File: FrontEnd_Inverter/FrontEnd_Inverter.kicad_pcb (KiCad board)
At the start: 4 copper layers, 210 x 127 mm, 80 parts, among them J1 Conn_02x20_Odd_Even, J11 CONN_02X06, P0 CONN_01X03, P10 CONN_01X02, P11 CONN_01X03, P20 CONN_01X02, P7 CONN_01X03, T1 SKiiP_13ACM12V18, U11 ACS758xCB-PFF, U12 ACS758xCB-PFF, U13 ACS758xCB-PFF, U14 ACS758xCB-PFF, U15 ACS758xCB-PFF, U30 ISE0505A-H, U40 ACPL-C87B, U50 ACPL-C87B

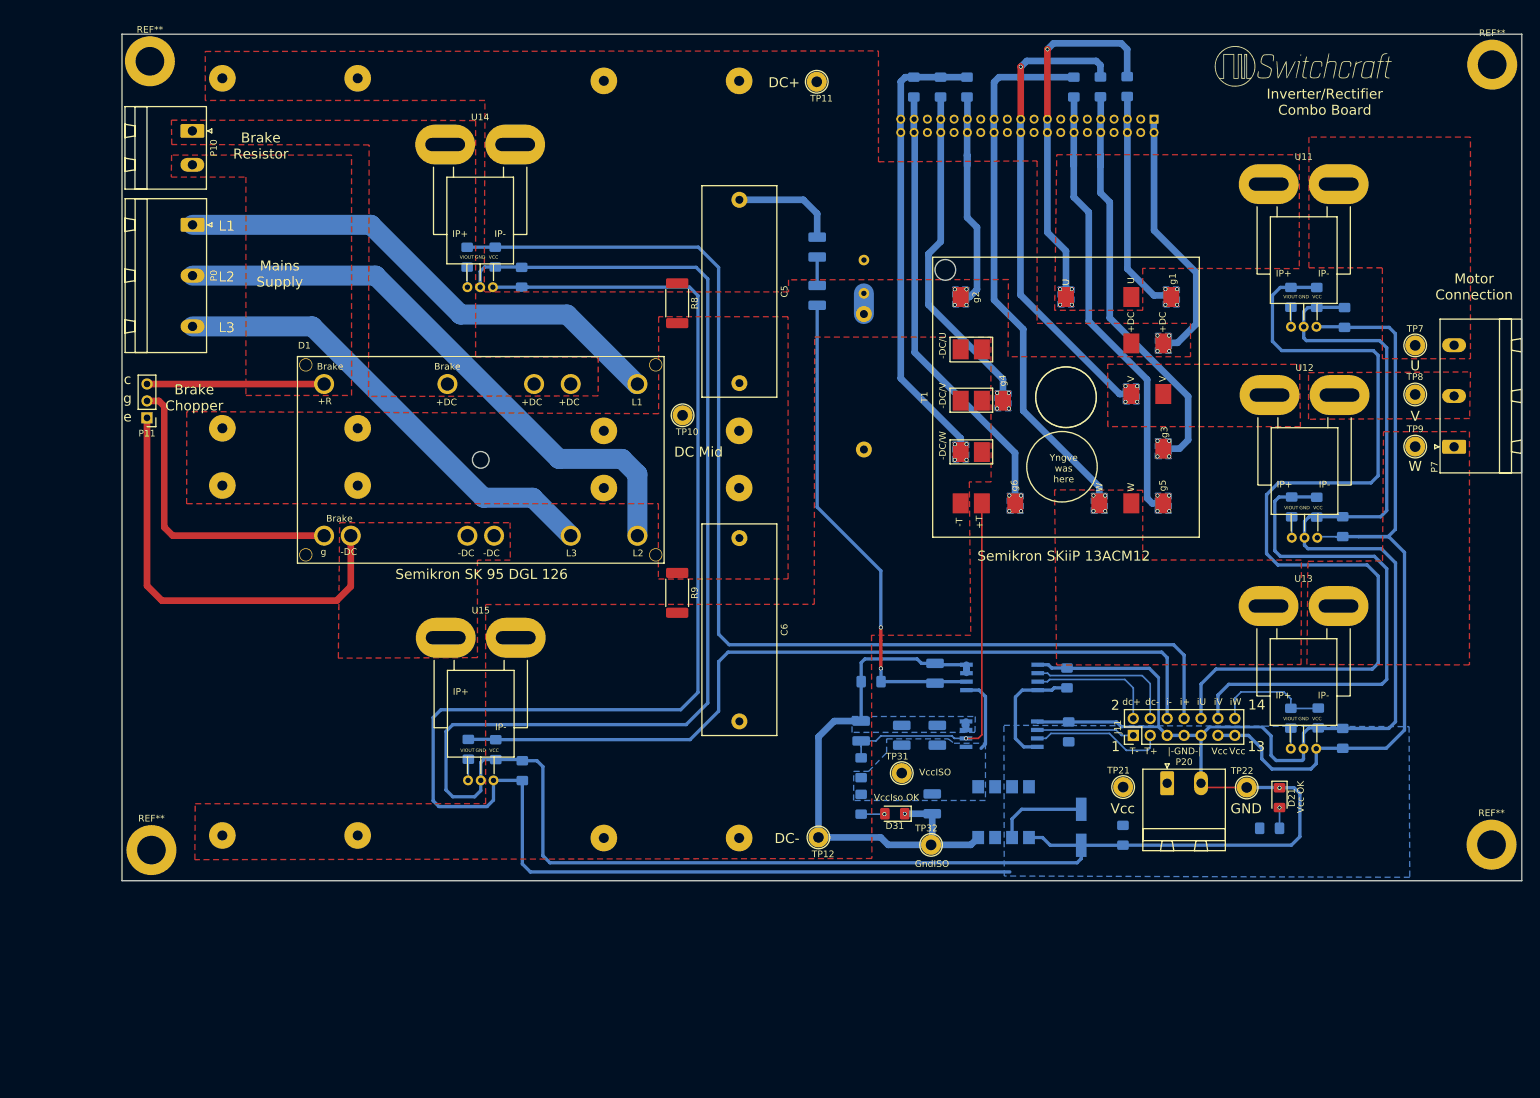
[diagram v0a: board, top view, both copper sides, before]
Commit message: Changed current sensor. Work in progress.
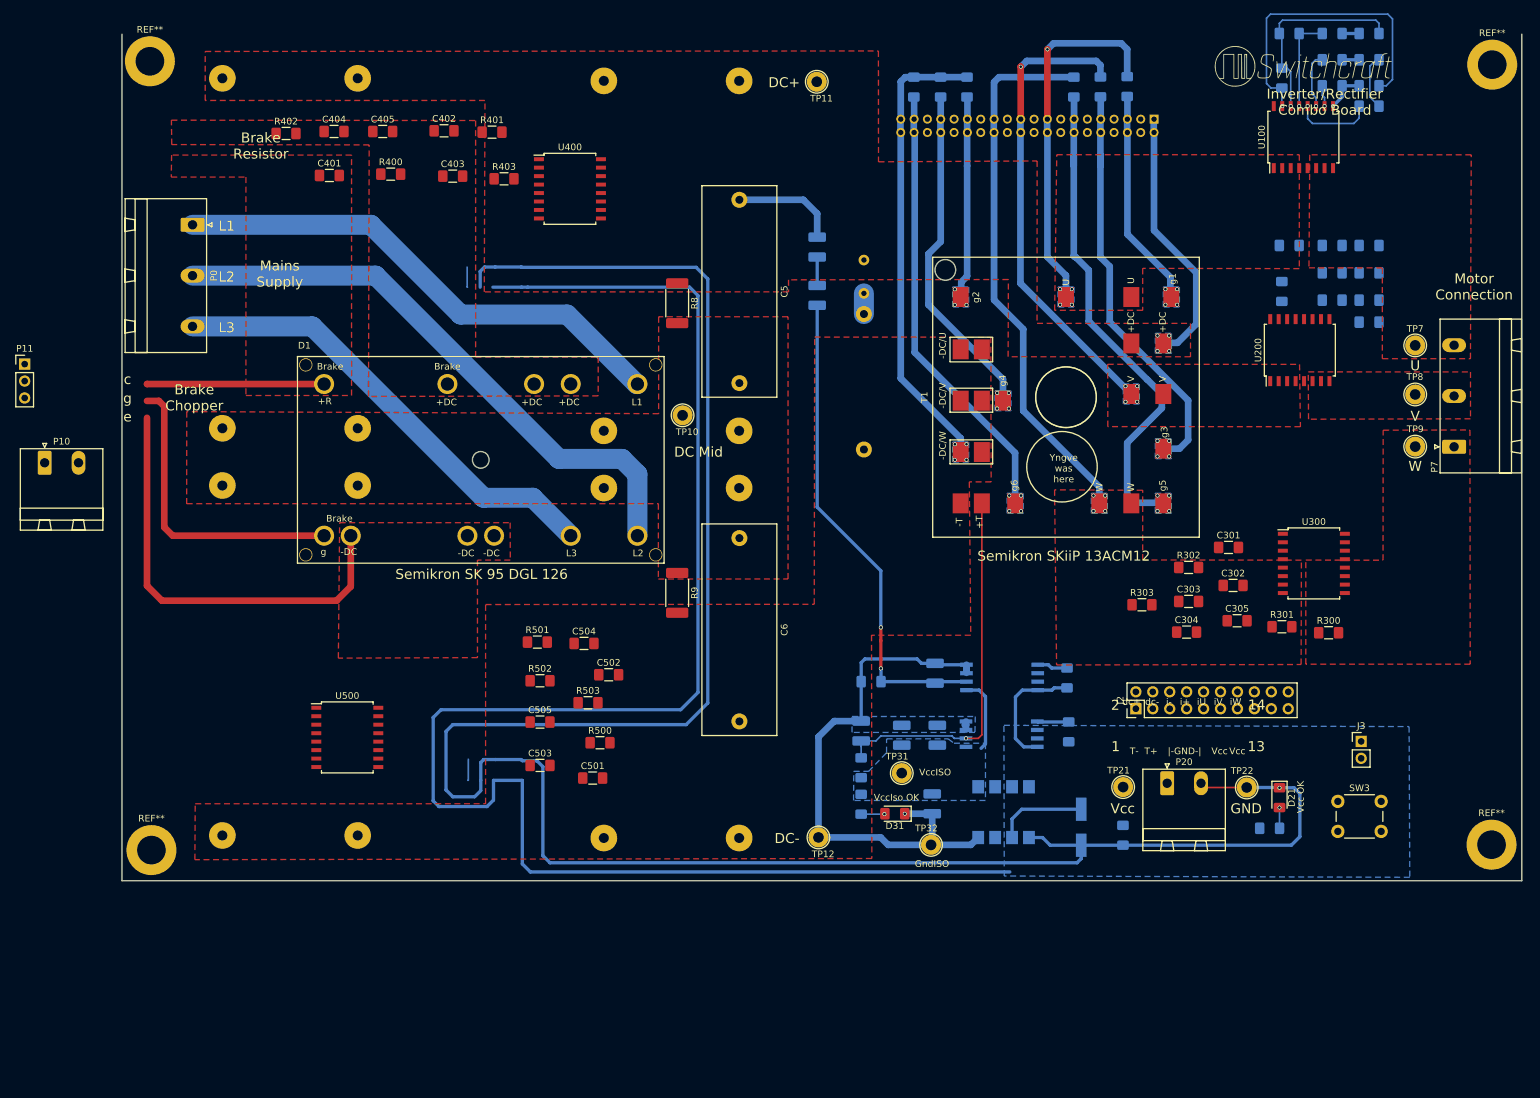
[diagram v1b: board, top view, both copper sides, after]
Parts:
- removed C11, C12, C13, C14, C15, C16, C17, C18, C19, C20: 100nF, Capacitor_SMD:C_1206_3216Metric_Pad1.42x1.75mm_HandSolder
- removed J11: CONN_02X06, Connector_PinHeader_2.54mm:PinHeader_2x07_P2.54mm_Vertical
- removed R11, R12, R13, R14, R15: 250, Resistor_SMD:R_1206_3216Metric_Pad1.42x1.75mm_HandSolder
- removed U11, U12, U13, U14, U15: ACS758xCB-PFF, Allegro:ACS758LCB-050B-PFF-T
- added C101: 1nF, Capacitor_SMD:C_1206_3216Metric_Pad1.42x1.75mm_HandSolder, B.Cu at (219.6, 23.7)
- added C102: 1nF, Capacitor_SMD:C_1206_3216Metric_Pad1.42x1.75mm_HandSolder, B.Cu at (219.6, 19.8)
- added C103: 22nF, Capacitor_SMD:C_1206_3216Metric_Pad1.42x1.75mm_HandSolder, B.Cu at (219.6, 15.9)
- added C104: 100nF, Capacitor_SMD:C_1206_3216Metric_Pad1.42x1.75mm_HandSolder, B.Cu at (225.1, 15.9)
- added C105: 100nF, Capacitor_SMD:C_1206_3216Metric_Pad1.42x1.75mm_HandSolder, B.Cu at (225.1, 19.8)
- added C201: 1nF, Capacitor_SMD:C_1206_3216Metric_Pad1.42x1.75mm_HandSolder, B.Cu at (219.6, 55.9)
- added C202: 1nF, Capacitor_SMD:C_1206_3216Metric_Pad1.42x1.75mm_HandSolder, B.Cu at (219.6, 51.8)
- added C203: 22nF, Capacitor_SMD:C_1206_3216Metric_Pad1.42x1.75mm_HandSolder, B.Cu at (219.6, 47.7)
- added C204: 100nF, Capacitor_SMD:C_1206_3216Metric_Pad1.42x1.75mm_HandSolder, B.Cu at (225.1, 47.7)
- added C205: 100nF, Capacitor_SMD:C_1206_3216Metric_Pad1.42x1.75mm_HandSolder, B.Cu at (225.1, 51.8)
- added C301: 1nF, Capacitor_SMD:C_1206_3216Metric_Pad1.42x1.75mm_HandSolder, F.Cu at (204.0, 93.0)
- added C302: 1nF, Capacitor_SMD:C_1206_3216Metric_Pad1.42x1.75mm_HandSolder, F.Cu at (204.7, 98.7)
- added C303: 22nF, Capacitor_SMD:C_1206_3216Metric_Pad1.42x1.75mm_HandSolder, F.Cu at (198.0, 101.1)
- added C304: 100nF, Capacitor_SMD:C_1206_3216Metric_Pad1.42x1.75mm_HandSolder, F.Cu at (197.7, 105.7)
- added C305: 100nF, Capacitor_SMD:C_1206_3216Metric_Pad1.42x1.75mm_HandSolder, F.Cu at (205.3, 104.0)
- added C401: 1nF, Capacitor_SMD:C_1206_3216Metric_Pad1.42x1.75mm_HandSolder, F.Cu at (69.1, 37.2)
- added C402: 1nF, Capacitor_SMD:C_1206_3216Metric_Pad1.42x1.75mm_HandSolder, F.Cu at (86.3, 30.5)
- added C403: 22nF, Capacitor_SMD:C_1206_3216Metric_Pad1.42x1.75mm_HandSolder, F.Cu at (87.6, 37.3)
- added C404: 100nF, Capacitor_SMD:C_1206_3216Metric_Pad1.42x1.75mm_HandSolder, F.Cu at (69.8, 30.6)
- added C405: 100nF, Capacitor_SMD:C_1206_3216Metric_Pad1.42x1.75mm_HandSolder, F.Cu at (77.1, 30.6)
- added C501: 1nF, Capacitor_SMD:C_1206_3216Metric_Pad1.42x1.75mm_HandSolder, F.Cu at (108.6, 127.6)
- added C502: 1nF, Capacitor_SMD:C_1206_3216Metric_Pad1.42x1.75mm_HandSolder, F.Cu at (111.0, 112.1)
- added C503: 22nF, Capacitor_SMD:C_1206_3216Metric_Pad1.42x1.75mm_HandSolder, F.Cu at (100.7, 125.7)
- added C504: 100nF, Capacitor_SMD:C_1206_3216Metric_Pad1.42x1.75mm_HandSolder, F.Cu at (107.3, 107.4)
- added C505: 100nF, Capacitor_SMD:C_1206_3216Metric_Pad1.42x1.75mm_HandSolder, F.Cu at (100.7, 119.2)
- added J2: Conn_02x10_Top_Bottom, Connector_PinHeader_2.54mm:PinHeader_2x10_P2.54mm_Vertical, F.Cu at (190.1, 117.2)
- added J3: Conn_01x02_Male, Connector_PinHeader_2.54mm:PinHeader_1x02_P2.54mm_Vertical, F.Cu at (223.9, 122.1)
- added R100: 250, Resistor_SMD:R_1206_3216Metric_Pad1.42x1.75mm_HandSolder, B.Cu at (225.1, 26.8)
- added R101: 2M, Resistor_SMD:R_1206_3216Metric_Pad1.42x1.75mm_HandSolder, B.Cu at (212.0, 22.6)
- added R102: 326k, Resistor_SMD:R_1206_3216Metric_Pad1.42x1.75mm_HandSolder, B.Cu at (225.1, 23.7)
- added R103: 330k, Resistor_SMD:R_1206_3216Metric_Pad1.42x1.75mm_HandSolder, B.Cu at (213.1, 15.9)
- added R200: 250, Resistor_SMD:R_1206_3216Metric_Pad1.42x1.75mm_HandSolder, B.Cu at (225.1, 59.2)
- added R201: 2M, Resistor_SMD:R_1206_3216Metric_Pad1.42x1.75mm_HandSolder, B.Cu at (212.0, 54.6)
- added R202: 326k, Resistor_SMD:R_1206_3216Metric_Pad1.42x1.75mm_HandSolder, B.Cu at (225.1, 55.9)
- added R203: 330k, Resistor_SMD:R_1206_3216Metric_Pad1.42x1.75mm_HandSolder, B.Cu at (213.1, 47.7)
- added R300: 250, Resistor_SMD:R_1206_3216Metric_Pad1.42x1.75mm_HandSolder, F.Cu at (219.0, 105.8)
- added R301: 2M, Resistor_SMD:R_1206_3216Metric_Pad1.42x1.75mm_HandSolder, F.Cu at (212.0, 104.9)
- added R302: 326k, Resistor_SMD:R_1206_3216Metric_Pad1.42x1.75mm_HandSolder, F.Cu at (198.0, 96.0)
- added R303: 330k, Resistor_SMD:R_1206_3216Metric_Pad1.42x1.75mm_HandSolder, F.Cu at (191.0, 101.6)
- added R400: 250, Resistor_SMD:R_1206_3216Metric_Pad1.42x1.75mm_HandSolder, F.Cu at (78.3, 37.0)
- added R401: 2M, Resistor_SMD:R_1206_3216Metric_Pad1.42x1.75mm_HandSolder, F.Cu at (93.5, 30.7)
- added R402: 326k, Resistor_SMD:R_1206_3216Metric_Pad1.42x1.75mm_HandSolder, F.Cu at (62.6, 30.9)
- added R403: 330k, Resistor_SMD:R_1206_3216Metric_Pad1.42x1.75mm_HandSolder, F.Cu at (95.3, 37.7)
- added R500: 250, Resistor_SMD:R_1206_3216Metric_Pad1.42x1.75mm_HandSolder, F.Cu at (109.7, 122.3)
- added R501: 2M, Resistor_SMD:R_1206_3216Metric_Pad1.42x1.75mm_HandSolder, F.Cu at (100.3, 107.2)
- added R502: 326k, Resistor_SMD:R_1206_3216Metric_Pad1.42x1.75mm_HandSolder, F.Cu at (100.7, 113.0)
- added R503: 330k, Resistor_SMD:R_1206_3216Metric_Pad1.42x1.75mm_HandSolder, F.Cu at (107.9, 116.3)
- added SW3: SW_Push_Open, Button_Switch_THT:SW_PUSH_6mm, F.Cu at (220.4, 131.1)
- added U100: ACS710KLATR-25CB, Package_SO:SOIC-16W_7.5x10.3mm_P1.27mm, F.Cu at (215.2, 31.4)
- added U200: ACS710KLATR-25CB, Package_SO:SOIC-16W_7.5x10.3mm_P1.27mm, F.Cu at (214.7, 63.4)
- added U300: ACS710KLATR-25CB, Package_SO:SOIC-16W_7.5x10.3mm_P1.27mm, F.Cu at (216.8, 95.4)
- added U400: ACS710KLATR-25CB, Package_SO:SOIC-16W_7.5x10.3mm_P1.27mm, F.Cu at (105.2, 39.2)
- added U500: ACS710KLATR-25CB, Package_SO:SOIC-16W_7.5x10.3mm_P1.27mm, F.Cu at (71.8, 121.5)
- TP7: value TEST -> U
- TP8: value TEST -> V
- TP9: value TEST -> W
- moved P10 54.5 mm to (26.4, 80.3), turned to 0 degrees
- moved P11 20.0 mm to (23.4, 65.5), turned to 0 degrees
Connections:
- net Net-(D1-Pad21) renamed DC-_in
- net Net-(D1-Pad4) renamed DC+_in
- net Net-(P7-Pad1) renamed W_out
- net Net-(P7-Pad2) renamed V_out
- net Net-(P7-Pad3) renamed U_out
- C1 pad 1: DC+ -> DC+_out
- C2 pad 2: GND_ISO -> DC-_out
- C22 pad 1: VCC -> DC-_out
- C3 pad 1: DC+ -> DC+_out
- C31 pad 2: GND_ISO -> DC-_out
- C4 pad 2: GND_ISO -> DC-_out
- C41 pad 1: Net-(C41-Pad1) -> DC-_out
- C41 pad 2: GND_ISO -> DC-_out
- C42 pad 1: GND_ISO -> DC-_out
- C43 pad 2: VCC -> DC-_out
- C5 pad 1: DC+ -> DC+_out
- C51 pad 2: GND_ISO -> DC-_out
- C52 pad 2: GND_ISO -> DC-_out
- C53 pad 1: VCC -> DC-_out
- C6 pad 2: GND_ISO -> DC-_out
- C7 pad 1: DC+ -> DC+_out
- CP21 pad 1: VCC -> DC-_out
- D31 pad 1: GND_ISO -> DC-_out
- J1 pad 1: DC+ -> DC+_out
- J1 pad 11: Net-(J1-Pad11) -> (no net)
- J1 pad 12: Net-(J1-Pad12) -> (no net)
- J1 pad 15: Net-(J1-Pad15) -> (no net)
- J1 pad 16: Net-(J1-Pad16) -> (no net)
- J1 pad 19: Net-(J1-Pad19) -> (no net)
- J1 pad 2: DC+ -> DC+_out
- J1 pad 20: Net-(J1-Pad20) -> (no net)
- J1 pad 23: Net-(J1-Pad23) -> (no net)
- J1 pad 24: Net-(J1-Pad24) -> (no net)
- J1 pad 27: Net-(J1-Pad27) -> (no net)
- J1 pad 28: Net-(J1-Pad28) -> (no net)
- J1 pad 3: Net-(J1-Pad3) -> (no net)
- J1 pad 31: Net-(J1-Pad31) -> (no net)
- J1 pad 32: Net-(J1-Pad32) -> (no net)
- J1 pad 35: Net-(J1-Pad35) -> (no net)
- J1 pad 36: Net-(J1-Pad36) -> (no net)
- J1 pad 39: GND_ISO -> DC-_out
- J1 pad 4: Net-(J1-Pad4) -> (no net)
- J1 pad 40: GND_ISO -> DC-_out
- J1 pad 7: Net-(J1-Pad7) -> (no net)
- J1 pad 8: Net-(J1-Pad8) -> (no net)
- P20 pad 1: VCC -> DC-_out
- R2 pad 2: GND_ISO -> DC-_out
- R21 pad 1: VCC -> DC-_out
- R4 pad 2: GND_ISO -> DC-_out
- R41 pad 1: Net-(C41-Pad1) -> DC-_out
- R51 pad 1: DC+ -> DC+_out
- R53 pad 2: GND_ISO -> DC-_out
- R6 pad 2: GND_ISO -> DC-_out
- R7 pad 2: GND_ISO -> DC-_out
- R8 pad 1: DC+ -> DC+_out
- R9 pad 2: GND_ISO -> DC-_out
- T1 pad 10: GND_ISO -> DC-_out
- T1 pad 11: GND_ISO -> DC-_out
- T1 pad 12: GND_ISO -> DC-_out
- T1 pad 13: GND_ISO -> DC-_out
- T1 pad 14: GND_ISO -> DC-_out
- T1 pad 21: Net-(C41-Pad1) -> DC-_out
- T1 pad 22: GND_ISO -> DC-_out
- T1 pad 9: GND_ISO -> DC-_out
- TP11 pad 1: DC+ -> DC+_out
- TP12 pad 1: GND_ISO -> DC-_out
- TP21 pad 1: VCC -> DC-_out
- TP32 pad 1: GND_ISO -> DC-_out
- U30 pad 2: VCC -> DC-_out
- U30 pad 4: GND_ISO -> DC-_out
- U30 pad 8: Net-(U30-Pad8) -> (no net)
- U40 pad 2: Net-(C41-Pad1) -> DC-_out
- U40 pad 3: GND_ISO -> DC-_out
- U40 pad 4: GND_ISO -> DC-_out
- U40 pad 6: T- -> DC-_out
- U40 pad 7: T+ -> (no net)
- U40 pad 8: VCC -> DC-_out
- U50 pad 3: GND_ISO -> DC-_out
- U50 pad 4: GND_ISO -> DC-_out
- U50 pad 8: VCC -> DC-_out
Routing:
- net DC-_out: track 0.00 -> 520.6 mm, vias 0 -> 7
- net VCC: track 402.8 -> 0.00 mm
- net GND: track 531.2 -> 352.5 mm, vias 1 -> 2
- net Net-(C17-Pad1): track 174.6 -> 0.00 mm
- net GND_ISO: track 153.7 -> 0.00 mm, vias 5 -> 0
- net Net-(C20-Pad1): track 139.9 -> 0.00 mm
- net Net-(C16-Pad1): track 124.1 -> 0.00 mm
- net Net-(C19-Pad1): track 78.5 -> 0.00 mm
- net Net-(C41-Pad1): track 56.1 -> 0.00 mm, vias 1 -> 0
- net DC+_out: track 0.00 -> 55.4 mm
- net DC+: track 55.4 -> 0.00 mm
- net Net-(R101-Pad1): track 0.00 -> 46.1 mm, vias 0 -> 1
- net Net-(J2-Pad2): track 22.8 -> 0.00 mm
- net T+: track 20.3 -> 0.00 mm
- net Net-(J2-Pad1): track 19.6 -> 0.00 mm
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- added copper zone on B.Cu, net (none)
- added copper zone on F.Cu, net (none)
- removed copper zone on F.Cu, net DC+_in
- removed copper zone on F.Cu, net DC-_in
- removed copper zone on F.Cu, net GND_ISO
- removed copper zone on F.Cu, net U_out
- removed copper zone on B.Cu, net VCC
- removed copper zone on F.Cu, net V_out
- removed copper zone on F.Cu, net W_out

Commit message: Further work on Inverter card. Schematic mostly done - still working on layout.
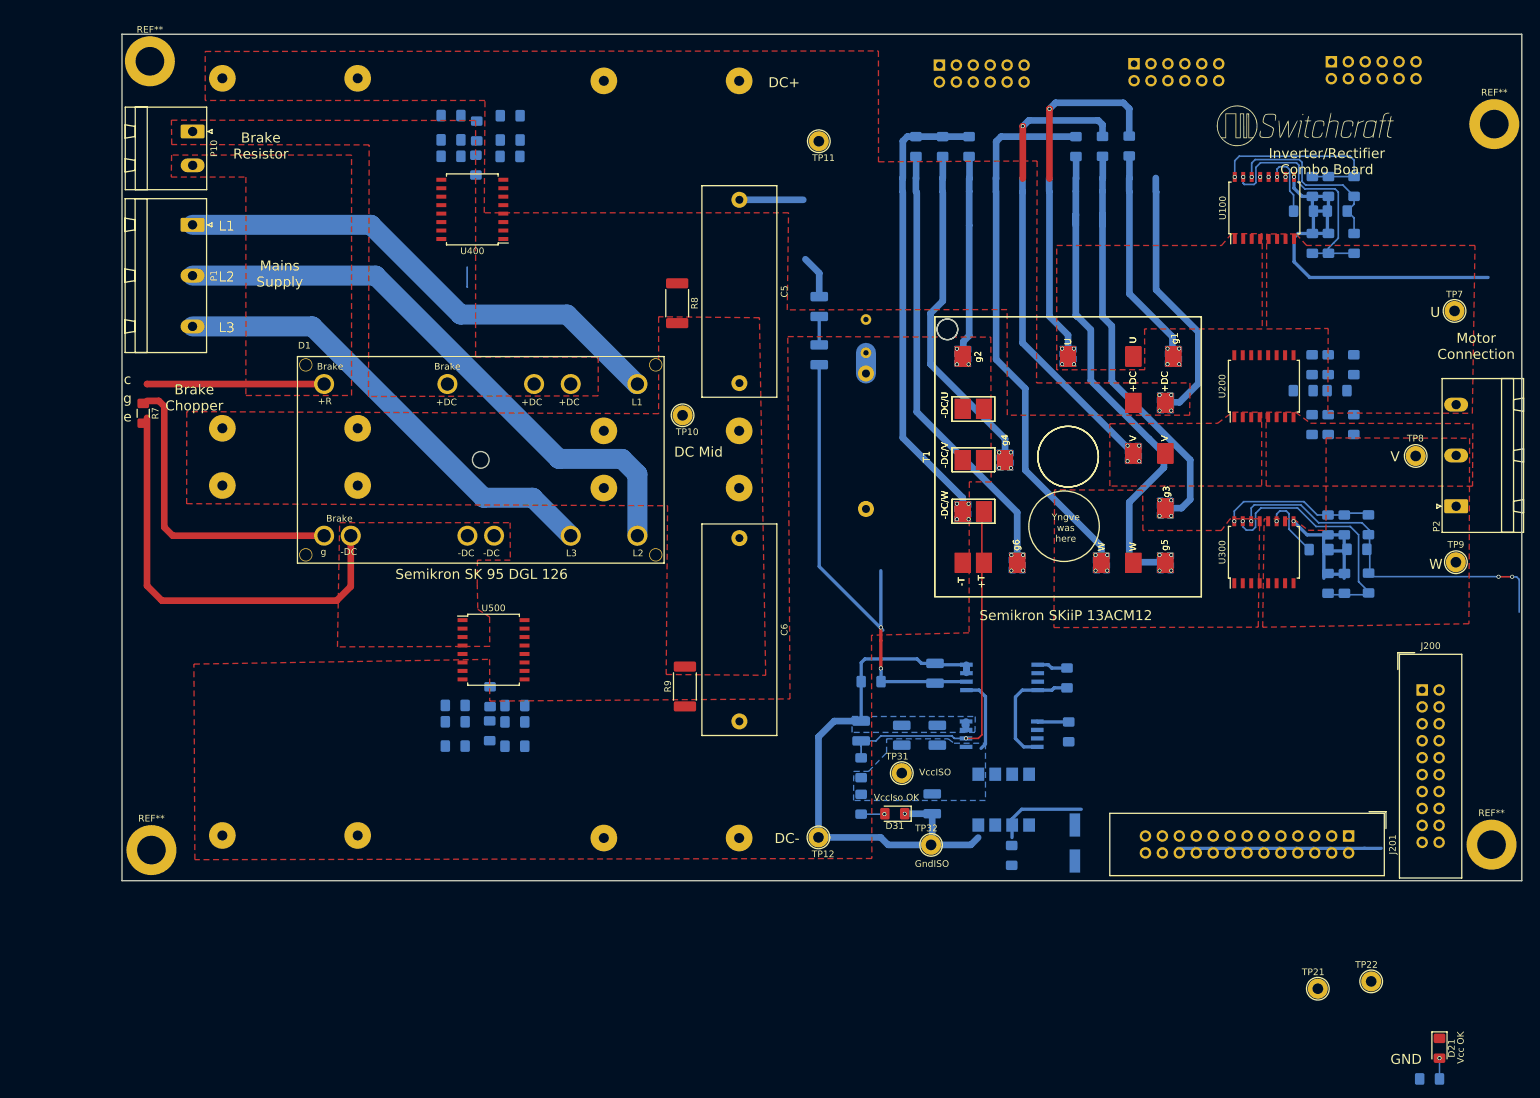
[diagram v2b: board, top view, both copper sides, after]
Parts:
- removed C104, C105, C204, C205, C304, C305, C404, C405, C505: 100nF, Capacitor_SMD:C_1206_3216Metric_Pad1.42x1.75mm_HandSolder
- removed P11: CONN_01X03, Connector_PinHeader_2.54mm:PinHeader_1x03_P2.54mm_Vertical
- removed P20: CONN_01X02, Connector_Phoenix_MSTB:PhoenixContact_MSTBA_2,5_2-G-5,08_1x02_P5.08mm_Horizontal
- removed R100, R200, R300, R400, R500: 250, Resistor_SMD:R_1206_3216Metric_Pad1.42x1.75mm_HandSolder
- removed SW3: SW_Push_Open, Button_Switch_THT:SW_PUSH_6mm
- added C100: 100nF, Capacitor_SMD:C_1206_3216Metric_Pad1.42x1.75mm_HandSolder, B.Cu at (220.3, 42.5)
- added C200: 100nF, Capacitor_SMD:C_1206_3216Metric_Pad1.42x1.75mm_HandSolder, B.Cu at (220.3, 69.5)
- added C300: 100nF, Capacitor_SMD:C_1206_3216Metric_Pad1.42x1.75mm_HandSolder, B.Cu at (223.3, 93.3)
- added C400: 100nF, Capacitor_SMD:C_1206_3216Metric_Pad1.42x1.75mm_HandSolder, B.Cu at (93.2, 120.5)
- added J200: AuxConnector_Analog, Connector_IDC:IDC-Header_2x10_P2.54mm_Vertical, F.Cu at (233.1, 114.4)
- added J201: DigOut_Connector, Connector_IDC:IDC-Header_2x13_P2.54mm_Vertical, F.Cu at (222.0, 136.3)
- added R104: 326k, Resistor_SMD:R_1206_3216Metric_Pad1.42x1.75mm_HandSolder, B.Cu at (219.0, 38.8)
- added R204: 326k, Resistor_SMD:R_1206_3216Metric_Pad1.42x1.75mm_HandSolder, B.Cu at (218.9, 65.6)
- added R304: 326k, Resistor_SMD:R_1206_3216Metric_Pad1.42x1.75mm_HandSolder, B.Cu at (221.4, 89.6)
- added R404: 326k, Resistor_SMD:R_1206_3216Metric_Pad1.42x1.75mm_HandSolder, B.Cu at (96.9, 119.2)
- added R504: 326k, Resistor_SMD:R_1206_3216Metric_Pad1.42x1.75mm_HandSolder, B.Cu at (87.4, 31.9)
- added R7: 100k, Resistor_SMD:R_1206_3216Metric_Pad1.42x1.75mm_HandSolder, F.Cu at (41.2, 72.9)
- added T1: SKiiP_13ACM12V18, Semikron:SKiiP_13ACM12V18, F.Cu at (179.9, 79.4)
- C103, C203: value 22nF -> 1nF
- C301, C302, C401, C402, C501, C502, R301, R302, R401, R402, R501, R502: moved to B.Cu
- C303, C403, C503: value 22nF -> 1nF; moved to B.Cu
- C500: renamed from C504; moved to B.Cu
- J1: value Conn_02x20_Odd_Even -> GateDriverConn; footprint Connector_PinSocket_2.00mm:PinSocket_2x20_P2.00mm_Vertical -> Connector_IDC:IDC-Header_2x06_P2.54mm_Vertical
- J2: value Conn_02x10_Top_Bottom -> GateDriverConn; footprint Connector_PinHeader_2.54mm:PinHeader_2x10_P2.54mm_Vertical -> Connector_IDC:IDC-Header_2x06_P2.54mm_Vertical; moved to B.Cu
- J3: value Conn_01x02_Male -> GateDriverConn; footprint Connector_PinHeader_2.54mm:PinHeader_1x02_P2.54mm_Vertical -> Connector_IDC:IDC-Header_2x06_P2.54mm_Vertical; moved to B.Cu
- R103, R203: value 330k -> 2M
- R303, R403, R503: value 330k -> 2M; moved to B.Cu
- U100, U200, U300, U400, U500: value ACS710KLATR-25CB -> ACS720KLATR-35B
- moved J3 119.6 mm to (160.6, 20.6), turned to 270 degrees
- moved J2 101.4 mm to (219.4, 20.1), turned to 270 degrees
- moved C501 94.1 mm to (96.2, 34.3), turned to 180 degrees
- moved R401 92.3 mm to (88.0, 122.8)
- moved R402 91.8 mm to (88.0, 119.2), turned to 180 degrees
- moved C503 90.6 mm to (91.1, 35.6), turned to 90 degrees
- moved R503 90.5 mm to (87.4, 28.2)
- moved C402 86.9 mm to (96.9, 116.7), turned to 180 degrees
- moved R403 85.1 mm to (96.9, 122.8), turned to 180 degrees
- moved C401 81.7 mm to (88.0, 116.7)
- moved C502 81.3 mm to (87.4, 34.3)
- moved R502 81.2 mm to (96.2, 31.9)
- moved R501 79.1 mm to (96.2, 28.2), turned to 180 degrees
- moved C500 78.5 mm to (91.2, 30.5), turned to 270 degrees
- moved C403 78.3 mm to (93.2, 115.4), turned to 270 degrees
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- renumbered P0 to P1, P7 to P2, R7 to R10, R3 to R2, R2 to R3, R5 to R4, R4 to R5
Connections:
- C1 pad 1: DC+_out -> +VDC
- C2 pad 2: DC-_out -> T-
- C22 pad 1: DC-_out -> VCC
- C3 pad 1: DC+_out -> +VDC
- C31 pad 2: DC-_out -> T-
- C4 pad 2: DC-_out -> T-
- C41 pad 1: DC-_out -> T+
- C41 pad 2: DC-_out -> T-
- C42 pad 1: DC-_out -> T-
- C43 pad 2: DC-_out -> VCC
- C5 pad 1: DC+_out -> +VDC
- C500 pad 1: DC-_out -> VCC
- C51 pad 2: DC-_out -> T-
- C52 pad 2: DC-_out -> T-
- C53 pad 1: DC-_out -> VCC
- C6 pad 2: DC-_out -> T-
- C7 pad 1: DC+_out -> +VDC
- CP21 pad 1: DC-_out -> VCC
- D1 pad 28: Net-(D1-Pad28) -> BC_gate
- D31 pad 1: DC-_out -> T-
- J1 pad 1: DC+_out -> +VDC
- J1 pad 10: T3_g -> DC-_out
- J1 pad 11: (no net) -> T2_g
- J1 pad 12: (no net) -> DC-_out
- J1 pad 2: DC+_out -> +VDC
- J1 pad 3: (no net) -> T1_g
- J1 pad 4: (no net) -> T1_g
- J1 pad 5: T1_g -> U
- J1 pad 6: T1_g -> U
- J1 pad 7: (no net) -> U
- J1 pad 8: (no net) -> U
- J1 pad 9: T3_g -> T2_g
- J2 pad 1: Net-(J2-Pad1) -> +VDC
- J2 pad 10: (no net) -> DC-_out
- J2 pad 11: Net-(C105-Pad1) -> T4_g
- J2 pad 12: Net-(C205-Pad1) -> DC-_out
- J2 pad 2: Net-(J2-Pad2) -> +VDC
- J2 pad 3: DC-_out -> T3_g
- J2 pad 4: DC-_out -> T3_g
- J2 pad 5: (no net) -> V
- J2 pad 6: (no net) -> V
- J2 pad 7: (no net) -> V
- J2 pad 8: (no net) -> V
- J2 pad 9: (no net) -> T4_g
- J3 pad 1: Net-(J3-Pad1) -> +VDC
- J3 pad 2: DC-_out -> +VDC
- R10 pad 2: DC-_out -> T-
- R101 pad 1: Net-(R101-Pad1) -> Net-(C101-Pad1)
- R101 pad 2: DC-_out -> VCC
- R102 pad 2: Net-(R101-Pad1) -> Net-(C101-Pad1)
- R103 pad 1: DC-_out -> Net-(C102-Pad1)
- R103 pad 2: Net-(C103-Pad1) -> VCC
- R2 pad 1: T3_g -> DC-_out
- R2 pad 2: V -> T2_g
- R201 pad 1: Net-(R201-Pad1) -> Net-(C201-Pad1)
- R201 pad 2: DC-_out -> VCC
- R202 pad 2: Net-(R201-Pad1) -> Net-(C201-Pad1)
- R203 pad 1: DC-_out -> Net-(C202-Pad1)
- R203 pad 2: Net-(C203-Pad1) -> VCC
- R21 pad 1: DC-_out -> VCC
- R3 pad 1: T2_g -> T3_g
- R3 pad 2: DC-_out -> V
- R301 pad 1: Net-(R301-Pad1) -> Net-(C301-Pad1)
- R301 pad 2: DC-_out -> VCC
- R302 pad 2: Net-(R301-Pad1) -> Net-(C301-Pad1)
- R303 pad 1: DC-_out -> Net-(C302-Pad1)
- R303 pad 2: Net-(C303-Pad1) -> VCC
- R4 pad 1: T5_g -> T4_g
- R4 pad 2: W -> DC-_out
- R401 pad 1: Net-(R401-Pad1) -> Net-(C401-Pad1)
- R401 pad 2: DC-_out -> VCC
- R402 pad 2: Net-(R401-Pad1) -> Net-(C401-Pad1)
- R403 pad 1: DC-_out -> Net-(C402-Pad1)
- R403 pad 2: Net-(C403-Pad1) -> VCC
- R41 pad 1: DC-_out -> T+
- R5 pad 1: T4_g -> T5_g
- R5 pad 2: DC-_out -> W
- R501 pad 1: Net-(R501-Pad1) -> Net-(C501-Pad1)
- R501 pad 2: DC-_out -> VCC
- R502 pad 2: Net-(R501-Pad1) -> Net-(C501-Pad1)
- R503 pad 1: DC-_out -> Net-(C502-Pad1)
- R503 pad 2: Net-(C503-Pad1) -> VCC
- R51 pad 1: DC+_out -> +VDC
- R53 pad 2: DC-_out -> T-
- R8 pad 1: DC+_out -> +VDC
- R9 pad 2: DC-_out -> T-
- TP11 pad 1: DC+_out -> +VDC
- TP12 pad 1: DC-_out -> T-
- TP21 pad 1: DC-_out -> VCC
- TP32 pad 1: DC-_out -> T-
- U100 pad 10: Net-(C101-Pad1) -> FAULT_S_U
- U100 pad 11: Net-(C102-Pad1) -> Net-(C103-Pad1)
- U100 pad 12: Net-(R100-Pad2) -> VI_U
- U100 pad 13: Net-(C103-Pad1) -> FAULT_F_U
- U100 pad 14: DC-_out -> VCC
- U100 pad 15: Net-(R101-Pad1) -> Net-(C101-Pad1)
- U100 pad 16: Rst -> Net-(C102-Pad1)
- U200 pad 10: Net-(C201-Pad1) -> FAULT_S_V
- U200 pad 11: Net-(C202-Pad1) -> Net-(C203-Pad1)
- U200 pad 12: Net-(R200-Pad2) -> VI_V
- U200 pad 13: Net-(C203-Pad1) -> FAULT_F_V
- U200 pad 14: DC-_out -> VCC
- U200 pad 15: Net-(R201-Pad1) -> Net-(C201-Pad1)
- U200 pad 16: Rst -> Net-(C202-Pad1)
- U30 pad 2: DC-_out -> VCC
- U30 pad 4: DC-_out -> T-
- U300 pad 10: Net-(C301-Pad1) -> FAULT_S_W
- U300 pad 11: Net-(C302-Pad1) -> Net-(C303-Pad1)
- U300 pad 12: Net-(R300-Pad2) -> VI_W
- U300 pad 13: Net-(C303-Pad1) -> FAULT_F_W
- U300 pad 14: DC-_out -> VCC
- U300 pad 15: Net-(R301-Pad1) -> Net-(C301-Pad1)
- U300 pad 16: Rst -> Net-(C302-Pad1)
- U40 pad 2: DC-_out -> T+
- U40 pad 3: DC-_out -> T-
- U40 pad 4: DC-_out -> T-
- U40 pad 6: DC-_out -> T-_out
- U40 pad 7: (no net) -> T+_out
- U40 pad 8: DC-_out -> VCC
- U400 pad 10: Net-(C401-Pad1) -> FAULT_S_DC+
- U400 pad 11: Net-(C402-Pad1) -> Net-(C403-Pad1)
- U400 pad 12: Net-(R400-Pad2) -> VI_DC+
- U400 pad 13: Net-(C403-Pad1) -> FAULT_F_DC+
- U400 pad 14: DC-_out -> VCC
- U400 pad 15: Net-(R401-Pad1) -> Net-(C401-Pad1)
- U400 pad 16: Rst -> Net-(C402-Pad1)
- U400 pad 5: DC+_out -> +VDC
- U400 pad 6: DC+_out -> +VDC
- U400 pad 7: DC+_out -> +VDC
- U400 pad 8: DC+_out -> +VDC
- U50 pad 3: DC-_out -> T-
- U50 pad 4: DC-_out -> T-
- U50 pad 6: Net-(J2-Pad2) -> DC_Meas-
- U50 pad 7: Net-(J2-Pad1) -> DC_Meas+
- U50 pad 8: DC-_out -> VCC
- U500 pad 10: Net-(C501-Pad1) -> FAULT_S_DC-
- U500 pad 11: Net-(C502-Pad1) -> Net-(C503-Pad1)
- U500 pad 12: Net-(R500-Pad2) -> VI_DC-
- U500 pad 13: Net-(C503-Pad1) -> FAULT_F_DC-
- U500 pad 14: DC-_out -> VCC
- U500 pad 15: Net-(R501-Pad1) -> Net-(C501-Pad1)
- U500 pad 16: Rst -> Net-(C502-Pad1)
- U500 pad 5: DC-_out -> T-
- U500 pad 6: DC-_out -> T-
- U500 pad 7: DC-_out -> T-
- U500 pad 8: DC-_out -> T-
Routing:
- net DC-_out: track 520.6 -> 270.5 mm, vias 7 -> 5
- net GND: track 352.5 -> 128.0 mm
- net VCC: track 0.00 -> 117.3 mm, vias 0 -> 4
- net T-: track 0.00 -> 84.2 mm, vias 0 -> 1
- net W: track 82.0 -> 0.00 mm
- net DC+_out: track 55.4 -> 0.00 mm
- net Net-(R101-Pad1): track 46.1 -> 0.00 mm, vias 1 -> 0
- net Net-(D1-Pad28): track 45.6 -> 0.00 mm
- net BC_gate: track 0.00 -> 45.6 mm
- net DC+: track 0.00 -> 39.3 mm
- net Net-(C301-Pad1): track 0.00 -> 39.1 mm, vias 0 -> 1
- net Net-(C101-Pad1): track 3.19 -> 37.4 mm
- net T3_g: track 63.0 -> 30.6 mm
- net T5_g: track 75.0 -> 51.0 mm
- net T4_g: track 51.0 -> 75.0 mm
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- added copper zone on F.Cu, net DC-_in
- added copper zone on F.Cu, net T-
- added copper zone on F.Cu, net U_out
- added copper zone on F.Cu, net V_out
- added copper zone on F.Cu, net W_out
- removed copper zone on F.Cu, net Net-(D1-Pad14)
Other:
- board text removed: "1"
- board text removed: "13"
- board text removed: "14"
- board text removed: "2"
- board text removed: "T+"
- board text removed: "T-"
- board text removed: "dc+"
- board text removed: "dc-"
- board text removed: "i+"
- board text removed: "i-"
- board text removed: "iU"
- board text removed: "iV"
- board text removed: "iW"
- board text removed: "|-GND-|"
